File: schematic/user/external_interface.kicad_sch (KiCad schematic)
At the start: 35 parts, among them J10 Radio Audio, J2 Radio_Jack, J3 User_Jack, J5 PTT Breakout, J9 User Audio, Q3 MBT3904DW1T1, Q4 MBT3904DW1T1, Q5 MBT3904DW1T1, SW3 PTT_Button, SW4 Mode_Button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

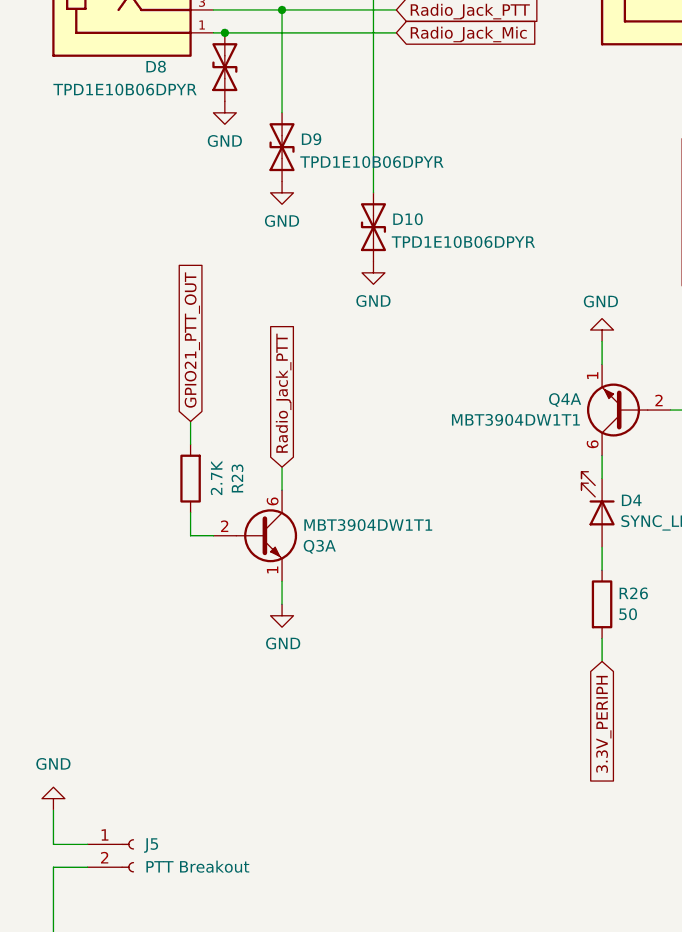
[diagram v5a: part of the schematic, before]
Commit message: v0.7 board: move NPN for PTT out to ensure low impedance path to GND when activated.
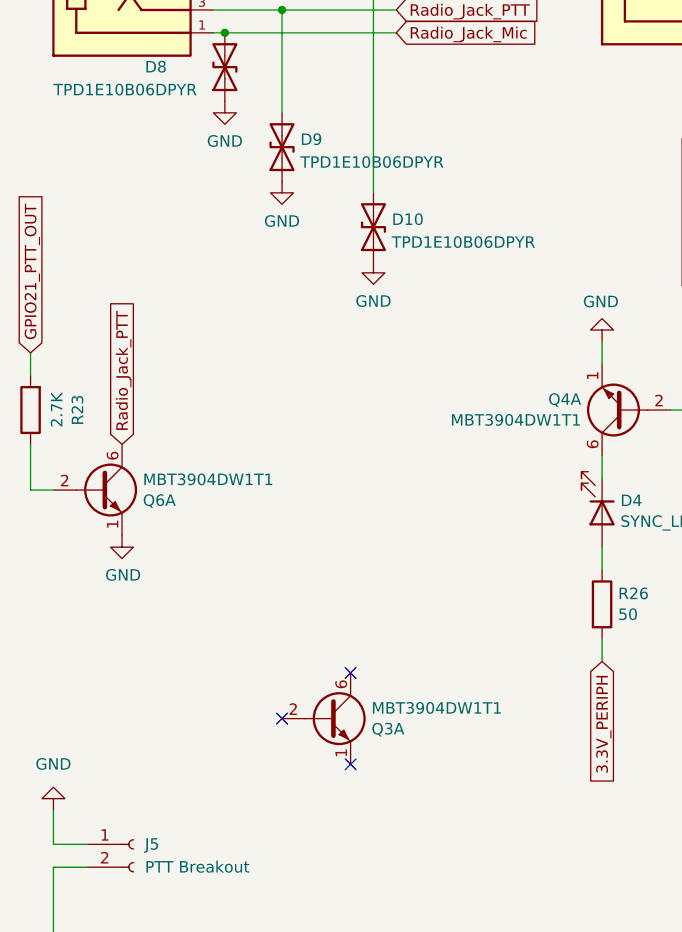
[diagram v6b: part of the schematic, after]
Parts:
- added Q6: MBT3904DW1T1, Package_TO_SOT_SMD:SOT-363_SC-70-6, symbol ezDV-rescue:Q_DUAL_NPN_NPN_E1B1C2E2B2C1-Device
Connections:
- net GND: now also Q6.1 (E1); no longer Q3.1 (E1)
- net Radio_Jack_PTT: now also Q6.6 (C1); no longer Q3.6 (C1)
- net at Q3.2 (B1): no longer R23.1
- new net: Q6.2 (B1), R23.1
- no-connect marks 0 -> 3
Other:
- moved on the sheet: Q3A, R23
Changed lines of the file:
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@@
   (junction (at 114.3 30.48) (diameter 0) (color 0 0 0 0)
   )
+  (no_connect (at 55.88 120.65))
+  (no_connect (at 48.26 115.57))
+  (no_connect (at 55.88 110.49))
   (wire (pts (xy 133.35 86.36) (xy 133.35 88.9))
     (stroke (width 0) (type default) (color 0 0 0 0))
@@
     (stroke (width 0) (type default) (color 0 0 0 0))
   )
-  (wire (pts (xy 48.26 90.17) (xy 48.26 87.63))
-    (stroke (width 0) (type default) (color 0 0 0 0))
-  )
   (wire (pts (xy 138.43 157.48) (xy 138.43 160.02))
     (stroke (width 0) (type default) (color 0 0 0 0))
@@
     (stroke (width 0) (type default) (color 0 0 0 0))
   )
-  (wire (pts (xy 38.1 85.09) (xy 38.1 82.55))
+  (wire (pts (xy 20.32 77.47) (xy 20.32 74.93))
     (stroke (width 0) (type default) (color 0 0 0 0))
   )
@@
     (stroke (width 0) (type default) (color 0 0 0 0))
   )
-  (wire (pts (xy 40.64 95.25) (xy 38.1 95.25))
-    (stroke (width 0) (type default) (color 0 0 0 0))
-  )
   (wire (pts (xy 116.84 49.53) (xy 116.84 35.56))
     (stroke (width 0) (type default) (color 0 0 0 0))
@@
     (stroke (width 0) (type default) (color 0 0 0 0))
   )
-  (wire (pts (xy 38.1 92.71) (xy 38.1 95.25))
+  (wire (pts (xy 20.32 85.09) (xy 20.32 90.17))
     (stroke (width 0) (type default) (color 0 0 0 0))
   )
@@
     (stroke (width 0) (type default) (color 0 0 0 0))
   )
+  (wire (pts (xy 22.86 90.17) (xy 20.32 90.17))
+    (stroke (width 0) (type default) (color 0 0 0 0))
+  )
   (wire (pts (xy 48.26 36.83) (xy 48.26 48.26))
     (stroke (width 0) (type default) (color 0 0 0 0))
@@
     (stroke (width 0) (type default) (color 0 0 0 0))
   )
-  (wire (pts (xy 48.26 100.33) (xy 48.26 102.87))
-    (stroke (width 0) (type default) (color 0 0 0 0))
-  )
   (wire (pts (xy 120.65 33.02) (xy 120.65 30.48))
     (stroke (width 0) (type default) (color 0 0 0 0))
@@
     )
   )
-  (global_label "Radio_Jack_PTT" (shape input) (at 48.26 87.63 90) (fields_autoplaced)
-    (effects (font (size 1.27 1.27)) (justify left))
-    (property "Intersheet References" "${INTERSHEET_REFS}" (id 0) (at -2.54 24.13 0)
+  (global_label "Radio_Jack_PTT" (shape input) (at 30.48 85.09 90) (fields_autoplaced)
+    (effects (font (size 1.27 1.27)) (justify left))
+    (property "Intersheet References" "${INTERSHEET_REFS}" (id 0) (at -20.32 21.59 0)
       (effects (font (size 1.27 1.27)) hide)
     )
@@
     )
   )
-  (global_label "GPIO21_PTT_OUT" (shape input) (at 38.1 82.55 90) (fields_autoplaced)
-    (effects (font (size 1.27 1.27)) (justify left))
-    (property "Intersheet References" "${INTERSHEET_REFS}" (id 0) (at -2.54 24.13 0)
+  (global_label "GPIO21_PTT_OUT" (shape input) (at 20.32 74.93 90) (fields_autoplaced)
+    (effects (font (size 1.27 1.27)) (justify left))
+    (property "Intersheet References" "${INTERSHEET_REFS}" (id 0) (at -20.32 16.51 0)
       (effects (font (size 1.27 1.27)) hide)
     )
@@
     (pin "1")
   )
-  (symbol (lib_id "ezDV-rescue:Q_DUAL_NPN_NPN_E1B1C2E2B2C1-Device") (at 45.72 95.25 0) (unit 1)
-    (in_bom yes) (on_board yes)
-    (property "Reference" "Q3" (id 0) (at 50.5714 96.4184 0)
-      (effects (font (size 1.27 1.27)) (justify left))
-    )
-    (property "Value" "MBT3904DW1T1" (id 1) (at 50.5714 94.107 0)
-      (effects (font (size 1.27 1.27)) (justify left))
-    )
-    (property "Footprint" "Package_TO_SOT_SMD:SOT-363_SC-70-6" (id 2) (at 50.8 92.71 0)
-      (effects (font (size 1.27 1.27)) hide)
-    )
-    (property "Datasheet" "https://datasheet.lcsc.com/lcsc/1811151434_onsemi-MBT3904DW1T1G_C110150.pdf" (id 3) (at 45.72 95.25 0)
-      (effects (font (size 1.27 1.27)) hide)
-    )
-    (property "LCSC" "C110150" (id 4) (at 45.72 95.25 0)
+  (symbol (lib_id "ezDV-rescue:Q_DUAL_NPN_NPN_E1B1C2E2B2C1-Device") (at 53.34 115.57 0) (unit 1)
+    (in_bom yes) (on_board yes)
+    (property "Reference" "Q3" (id 0) (at 58.1914 116.7384 0)
+      (effects (font (size 1.27 1.27)) (justify left))
+    )
+    (property "Value" "MBT3904DW1T1" (id 1) (at 58.1914 114.427 0)
+      (effects (font (size 1.27 1.27)) (justify left))
+    )
+    (property "Footprint" "Package_TO_SOT_SMD:SOT-363_SC-70-6" (id 2) (at 58.42 113.03 0)
+      (effects (font (size 1.27 1.27)) hide)
+    )
+    (property "Datasheet" "https://datasheet.lcsc.com/lcsc/1811151434_onsemi-MBT3904DW1T1G_C110150.pdf" (id 3) (at 53.34 115.57 0)
+      (effects (font (size 1.27 1.27)) hide)
+    )
+    (property "LCSC" "C110150" (id 4) (at 53.34 115.57 0)
       (effects (font (size 1.27 1.27)) hide)
     )
@@
     (pin "2")
   )
-  (symbol (lib_id "Device:R") (at 38.1 88.9 180) (unit 1)
-    (in_bom yes) (on_board yes)
-    (property "Reference" "R23" (id 0) (at 43.3578 88.9 90))
-    (property "Value" "2.7K" (id 1) (at 41.0464 88.9 90))
-    (property "Footprint" "Resistor_SMD:R_0603_1608Metric" (id 2) (at 39.878 88.9 90)
-      (effects (font (size 1.27 1.27)) hide)
-    )
-    (property "Datasheet" "https://datasheet.lcsc.com/lcsc/2206010216_UNI-ROYAL-Uniroyal-Elec-0603WAF2701T5E_C13167.pdf" (id 3) (at 38.1 88.9 0)
-      (effects (font (size 1.27 1.27)) hide)
-    )
-    (property "LCSC" "C13167" (id 4) (at 38.1 88.9 0)
+  (symbol (lib_id "Device:R") (at 20.32 81.28 180) (unit 1)
+    (in_bom yes) (on_board yes)
+    (property "Reference" "R23" (id 0) (at 25.5778 81.28 90))
+    (property "Value" "2.7K" (id 1) (at 23.2664 81.28 90))
+    (property "Footprint" "Resistor_SMD:R_0603_1608Metric" (id 2) (at 22.098 81.28 90)
+      (effects (font (size 1.27 1.27)) hide)
+    )
+    (property "Datasheet" "https://datasheet.lcsc.com/lcsc/2206010216_UNI-ROYAL-Uniroyal-Elec-0603WAF2701T5E_C13167.pdf" (id 3) (at 20.32 81.28 0)
+      (effects (font (size 1.27 1.27)) hide)
+    )
+    (property "LCSC" "C13167" (id 4) (at 20.32 81.28 0)
       (effects (font (size 1.27 1.27)) hide)
     )
@@
     (pin "4")
   )
-  (symbol (lib_id "power:GND") (at 48.26 102.87 0) (unit 1)
-    (in_bom yes) (on_board yes)
-    (property "Reference" "#PWR028" (id 0) (at 48.26 109.22 0)
-      (effects (font (size 1.27 1.27)) hide)
-    )
-    (property "Value" "GND" (id 1) (at 48.387 107.2642 0))
-    (property "Footprint" "" (id 2) (at 48.26 102.87 0)
-      (effects (font (size 1.27 1.27)) hide)
-    )
-    (property "Datasheet" "" (id 3) (at 48.26 102.87 0)
+  (symbol (lib_id "power:GND") (at 30.48 95.25 0) (unit 1)
+    (in_bom yes) (on_board yes)
+    (property "Reference" "#PWR028" (id 0) (at 30.48 101.6 0)
+      (effects (font (size 1.27 1.27)) hide)
+    )
+    (property "Value" "GND" (id 1) (at 30.607 99.6442 0))
+    (property "Footprint" "" (id 2) (at 30.48 95.25 0)
+      (effects (font (size 1.27 1.27)) hide)
+    )
+    (property "Datasheet" "" (id 3) (at 30.48 95.25 0)
       (effects (font (size 1.27 1.27)) hide)
     )
@@
     (pin "2")
   )
+  (symbol (lib_id "ezDV-rescue:Q_DUAL_NPN_NPN_E1B1C2E2B2C1-Device") (at 27.94 90.17 0) (unit 1)
+    (in_bom yes) (on_board yes)
+    (property "Reference" "Q6" (id 0) (at 32.7914 91.3384 0)
+      (effects (font (size 1.27 1.27)) (justify left))
+    )
+    (property "Value" "MBT3904DW1T1" (id 1) (at 32.7914 89.027 0)
+      (effects (font (size 1.27 1.27)) (justify left))
+    )
+    (property "Footprint" "Package_TO_SOT_SMD:SOT-363_SC-70-6" (id 2) (at 33.02 87.63 0)
+      (effects (font (size 1.27 1.27)) hide)
+    )
+    (property "Datasheet" "https://datasheet.lcsc.com/lcsc/1811151434_onsemi-MBT3904DW1T1G_C110150.pdf" (id 3) (at 27.94 90.17 0)
+      (effects (font (size 1.27 1.27)) hide)
+    )
+    (property "LCSC" "C110150" (id 4) (at 27.94 90.17 0)
+      (effects (font (size 1.27 1.27)) hide)
+    )
+    (pin "1")
+    (pin "2")
+    (pin "6")
+    (pin "3")
+    (pin "4")
+    (pin "5")
+  )
   (symbol (lib_id "Device:LED") (at 162.56 85.09 270) (unit 1)
